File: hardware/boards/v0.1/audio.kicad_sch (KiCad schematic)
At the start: 46 parts, among them J4 SPKR_L, J5 SPKR_R, J7 HP, J8 LINE_OUT, J9 LINE_IN, U24 MIC, U28 TS5A23159RSE, U29 NAU88C22YG, U34 SI4710-B30-GMR, U35 SI4703-C19-GMR, Y3 ASVK-32.768KHZ-LJ-T

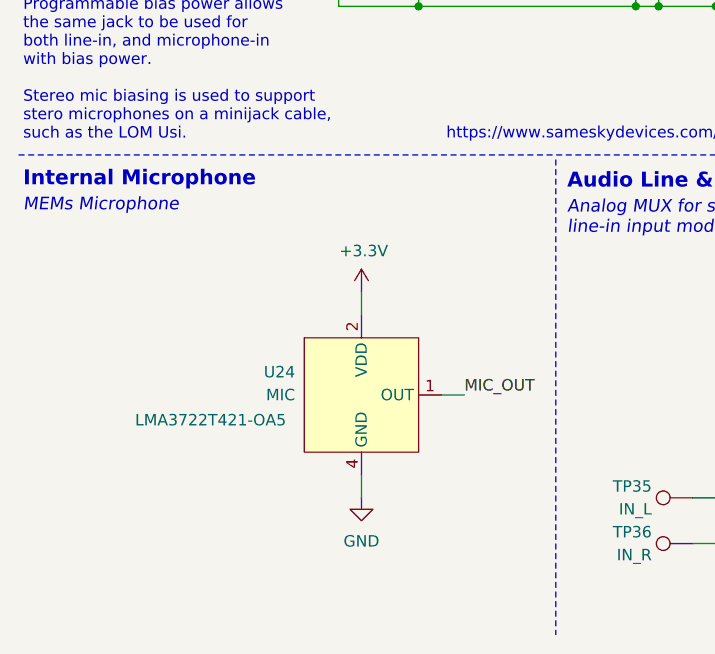
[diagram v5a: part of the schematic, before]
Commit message: feat: add haptic transducer DAC
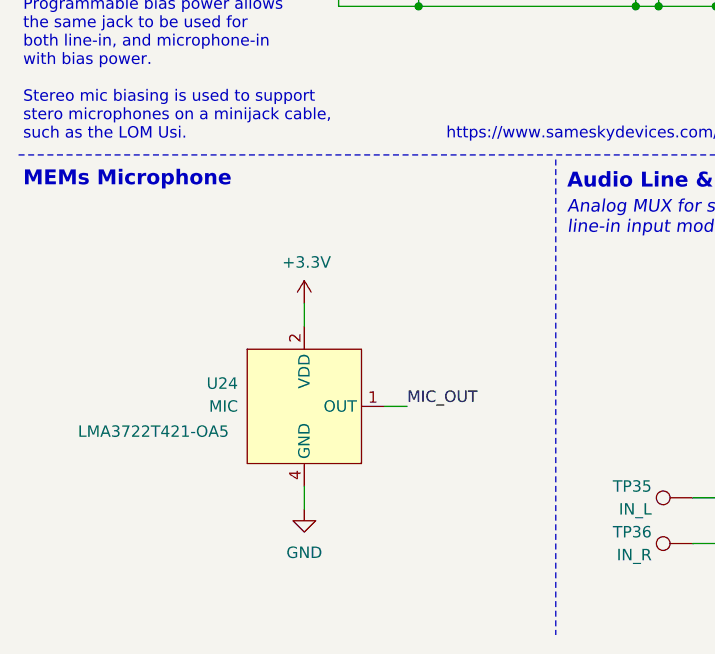
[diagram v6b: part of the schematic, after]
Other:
- note removed: "Internal Microphone"
- moved on the sheet: U24
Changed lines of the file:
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@@
 		)
 	)
-	(text "MEMs Microphone"
-		(exclude_from_sim no)
-		(at 13.208 149.606 0)
-		(effects
-			(font
-				(size 1.397 1.397)
-				(italic yes)
-				(color 194 194 194 1)
-			)
-			(justify left top)
-		)
-	)
 	(text "Headphone antenna: AN383 P.g. 13\nIdeal with cables 1.1 to 1.45m"
 		(exclude_from_sim no)
@@
 		)
 	)
-	(text "Internal Microphone"
+	(text "MEMs Microphone"
 		(exclude_from_sim no)
 		(at 13.208 146.558 0)
@@
 	(wire
 		(pts
-			(xy 59.69 171.45) (xy 62.23 171.45)
+			(xy 53.34 172.72) (xy 55.88 172.72)
 		)
 		(stroke
@@
 	(wire
 		(pts
-			(xy 50.8 160.02) (xy 50.8 162.56)
+			(xy 44.45 161.29) (xy 44.45 163.83)
 		)
 		(stroke
@@
 	(wire
 		(pts
-			(xy 50.8 180.34) (xy 50.8 182.88)
+			(xy 44.45 181.61) (xy 44.45 184.15)
 		)
 		(stroke
@@
 	)
 	(label "MIC_OUT"
-		(at 62.23 171.45 0)
+		(at 55.88 172.72 0)
 		(effects
 			(font
@@
 	(symbol
 		(lib_id "power:GND")
-		(at 50.8 182.88 0)
+		(at 44.45 184.15 0)
 		(unit 1)
 		(exclude_from_sim no)
@@
 		(dnp no)
 		(property "Reference" "#PWR057"
-			(at 50.8 189.23 0)
+			(at 44.45 190.5 0)
 			(effects
 				(font
@@
 		)
 		(property "Value" "GND"
-			(at 50.8 187.706 0)
+			(at 44.45 188.976 0)
 			(effects
 				(font
@@
 		)
 		(property "Footprint" ""
-			(at 50.8 182.88 0)
+			(at 44.45 184.15 0)
 			(effects
 				(font
@@
 		)
 		(property "Datasheet" ""
-			(at 50.8 182.88 0)
+			(at 44.45 184.15 0)
 			(effects
 				(font
@@
 		)
 		(property "Description" "Power symbol creates a global label with name \"GND\" , ground"
-			(at 50.8 182.88 0)
+			(at 44.45 184.15 0)
 			(effects
 				(font
@@
 	(symbol
 		(lib_id "pocket_synth:LMA3722T421-OA5")
-		(at 50.8 171.45 0)
+		(at 44.45 172.72 0)
 		(unit 1)
 		(exclude_from_sim no)
@@
 		(dnp no)
 		(property "Reference" "U24"
-			(at 43.434 168.91 0)
+			(at 37.084 170.18 0)
 			(effects
 				(font
@@
 		)
 		(property "Value" "MIC"
-			(at 43.434 171.45 0)
+			(at 37.084 172.72 0)
 			(effects
 				(font
@@
 		)
 		(property "Footprint" "pocket_synth:LMA3722T421-OA5"
-			(at 50.8 171.45 0)
+			(at 44.45 172.72 0)
 			(effects
 				(font
@@
 		)
 		(property "Datasheet" "https://jlcpcb.com/api/file/downloadByFileSystemAccessId/8603050779259248640"
-			(at 50.8 171.45 0)
+			(at 44.45 172.72 0)
 			(effects
 				(font
@@
 		)
 		(property "Description" "LMA3722T421-OA5"
-			(at 34.036 174.244 0)
+			(at 27.686 175.514 0)
 			(effects
 				(font
@@
 		)
 		(property "JLC" "C5373233"
-			(at 50.8 171.45 0)
+			(at 44.45 172.72 0)
 			(effects
 				(font
@@
 		)
 		(property "MANUFACTURER" ""
-			(at 50.8 171.45 0)
+			(at 44.45 172.72 0)
 			(effects
 				(font
@@
 		)
 		(property "MAXIMUM_PACKAGE_HEIGHT" ""
-			(at 50.8 171.45 0)
+			(at 44.45 172.72 0)
 			(effects
 				(font
@@
 		)
 		(property "Connector" ""
-			(at 50.8 171.45 0)
+			(at 44.45 172.72 0)
 			(effects
 				(font
@@
 	(symbol
 		(lib_id "power:+3.3V")
-		(at 50.8 160.02 0)
+		(at 44.45 161.29 0)
 		(unit 1)
 		(exclude_from_sim no)
@@
 		(dnp no)
 		(property "Reference" "#PWR068"
-			(at 50.8 163.83 0)
+			(at 44.45 165.1 0)
 			(effects
 				(font
@@
 		)
 		(property "Value" "+3.3V"
-			(at 51.054 155.448 0)
+			(at 44.704 156.718 0)
 			(effects
 				(font
@@
 		)
 		(property "Footprint" ""
-			(at 50.8 160.02 0)
+			(at 44.45 161.29 0)
 			(effects
 				(font
@@
 		)
 		(property "Datasheet" ""
-			(at 50.8 160.02 0)
+			(at 44.45 161.29 0)
 			(effects
 				(font
@@
 		)
 		(property "Description" "Power symbol creates a global label with name \"+3.3V\""
-			(at 50.8 160.02 0)
+			(at 44.45 161.29 0)
 			(effects
 				(font

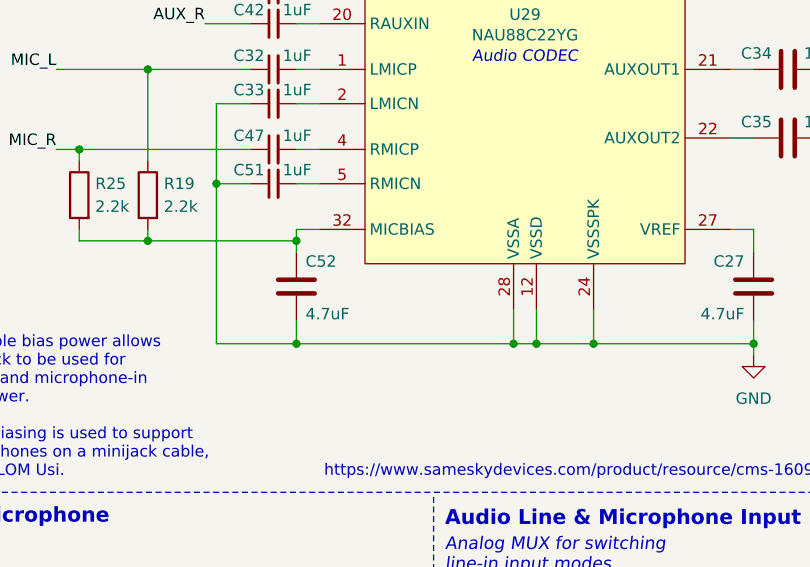
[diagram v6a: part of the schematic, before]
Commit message: feat: reduce via-in-pads
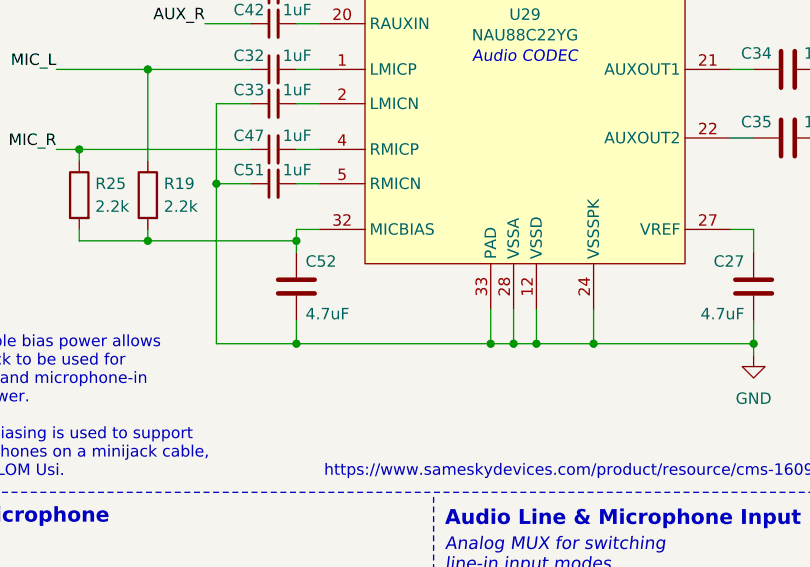
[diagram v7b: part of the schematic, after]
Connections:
- net EPAD: now also U29.33 (PAD)
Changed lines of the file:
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@@
 	)
 	(junction
+		(at 78.74 128.27)
+		(diameter 0)
+		(color 0 0 0 0)
+	)
+	(junction
 		(at 83.82 128.27)
 		(diameter 0)
@@
 	(wire
 		(pts
+			(xy 78.74 124.46) (xy 78.74 128.27)
+		)
+		(stroke
+			(width 0)
+			(type default)
+		)
+	)
+	(wire
+		(pts
 			(xy 250.19 110.49) (xy 256.54 110.49)
 		)
@@
 	(wire
 		(pts
+			(xy 78.74 128.27) (xy 81.28 128.27)
+		)
+		(stroke
+			(width 0)
+			(type default)
+		)
+	)
+	(wire
+		(pts
 			(xy 246.38 78.74) (xy 246.38 80.01)
 		)
@@
 	(wire
 		(pts
-			(xy 57.15 128.27) (xy 81.28 128.27)
+			(xy 57.15 128.27) (xy 78.74 128.27)
 		)
 		(stroke
@@
 		(pin "15"
 		)
+		(pin "33"
+		)
 		(instances

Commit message: feat: change charger, fuel gauge, and battery connector, re-route power system
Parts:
- C32, C33, C34, C35, C38, C42, C47, C51: JLC C14445 -> C52923
- R10, R51: JLC C25531 -> C25744
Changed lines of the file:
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@@
 			)
 		)
-		(property "JLC" "C14445"
+		(property "JLC" "C52923"
 			(at 54.61 88.9 0)
 			(effects
@@
 			)
 		)
-		(property "JLC" "C25531"
+		(property "JLC" "C25744"
 			(at 142.24 172.72 0)
 			(effects
@@
 			)
 		)
-		(property "JLC" "C14445"
+		(property "JLC" "C52923"
 			(at 111.76 97.79 0)
 			(effects
@@
 			)
 		)
-		(property "JLC" "C14445"
+		(property "JLC" "C52923"
 			(at 111.76 105.41 0)
 			(effects
@@
 			)
 		)
-		(property "JLC" "C14445"
+		(property "JLC" "C52923"
 			(at 54.61 106.68 0)
 			(effects
@@
 			)
 		)
-		(property "JLC" "C14445"
+		(property "JLC" "C52923"
 			(at 54.61 97.79 0)
 			(effects
@@
 			)
 		)
-		(property "JLC" "C14445"
+		(property "JLC" "C52923"
 			(at 54.61 101.6 0)
 			(effects
@@
 			)
 		)
-		(property "JLC" "C14445"
+		(property "JLC" "C52923"
 			(at 54.61 110.49 0)
 			(effects
@@
 			)
 		)
-		(property "JLC" "C25531"
+		(property "JLC" "C25744"
 			(at 129.54 175.26 0)
 			(effects
@@
 			)
 		)
-		(property "JLC" "C14445"
+		(property "JLC" "C52923"
 			(at 54.61 92.71 0)
 			(effects
